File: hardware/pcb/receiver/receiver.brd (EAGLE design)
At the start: 100 x 100 mm, 82 parts, among them X1 5-1634506-1H

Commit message: hw: receiver board changes
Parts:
- removed C17, C23: 100n, rcl:C0805
- removed L6: ferrite bead, inductor-neosid:SM-NE29
- moved R8 148.2 mm to (71.1, 73.7), turned to 180 degrees
- moved C43 142.8 mm to (65.7, 60.5)
- moved R7 141.1 mm to (69.1, 71.1), turned to 180 degrees
- moved C4 140.4 mm to (84.5, 27.1), turned to 270 degrees
- moved C38 139.6 mm to (70.6, 39.7), turned to 90 degrees
- moved C5 133.9 mm to (73.4, 39.6), turned to 90 degrees
- moved C35 132.7 mm to (70.6, 56.9), turned to 90 degrees
- moved C29 129.0 mm to (61.5, 45.7), flipped to the bottom, turned to 180 degrees
- moved C28 126.4 mm to (65.6, 42.3), flipped to the bottom
- moved IC5 125.2 mm to (68.5, 48.0)
- moved C2 122.5 mm to (80.6, 64.8), turned to 180 degrees
- moved L7 122.0 mm to (65.0, 66.4), turned to 180 degrees
- moved C42 122.0 mm to (81.7, 27.4), turned to 270 degrees
- moved C3 121.0 mm to (72.9, 56.6), turned to 270 degrees
- moved C27 118.1 mm to (64.1, 55.2), flipped to the bottom, turned to 90 degrees
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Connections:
- removed net N$35: SV1.2
- net +3V3: no longer C17.2, C42.2, JP1.1, L6.2, R11.2, R12.2, R7.2, V1.8
- net +3V3A_ADC: now also JP1.1, R11.2, R12.2, R7.2; no longer C23.2
- net AMPOUT_N: now also IC2.4, R2.1; no longer IC2.5, R1.1
- net AMPOUT_P: now also IC2.5, R1.1; no longer IC2.4, R2.1
- net ENC: now also SV1.2; no longer SV1.8
- net ENC_N: now also IC5.12; no longer IC5.13
- net ENC_P: now also IC5.13; no longer IC5.12
- net GND: no longer C17.1, C23.1
- net IN_N: now also IC5.9, R2.2; no longer IC5.8, R1.2
- net IN_P: now also IC5.8, R1.2; no longer IC5.9, R2.2
- net N$4: now also IC2.8; no longer IC2.1
- net N$5: now also IC2.1; no longer IC2.8
- net VDD: now also C42.2, V1.8; no longer L6.1
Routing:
- net IN_N: track 0.00 -> 0.55 mm
- added copper zone on layer 1, net GND

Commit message: hw: receiver ferrite beads between capacitors
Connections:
- net +3V3: now also C43.1
- net +3V3A_ADC: no longer C43.1
- net +5V: now also C41.1
- net +5V_AMP: no longer C41.1
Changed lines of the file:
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@@
 <contactref element="L4" pad="1"/>
 <contactref element="L7" pad="2"/>
+<contactref element="C43" pad="1"/>
 <wire x1="77.528" y1="61.266" x2="79.674" y2="64.808" width="0" layer="19" extent="1-1"/>
-<wire x1="63.802" y1="66.428" x2="77.528" y2="61.266" width="0" layer="19" extent="1-1"/>
+<wire x1="64.798" y1="60.46" x2="77.528" y2="61.266" width="0" layer="19" extent="1-1"/>
+<wire x1="63.802" y1="66.428" x2="64.798" y2="60.46" width="0" layer="19" extent="1-1"/>
 <wire x1="47.55" y1="88" x2="63.802" y2="66.428" width="0" layer="19" extent="1-1"/>
 <wire x1="45" y1="88.45" x2="47.55" y2="88" width="0" layer="19" extent="1-1"/>
@@
 <contactref element="C29" pad="2"/>
 <contactref element="L7" pad="1"/>
-<contactref element="C43" pad="1"/>
 <contactref element="IC5" pad="1"/>
 <contactref element="JP1" pad="1"/>
@@
 <wire x1="69.342" y1="67.482" x2="68.138" y2="71.12" width="0" layer="19" extent="1-1"/>
 <wire x1="66.102" y1="66.428" x2="69.342" y2="67.482" width="0" layer="19" extent="1-1"/>
-<wire x1="64.798" y1="60.46" x2="66.102" y2="66.428" width="0" layer="19" extent="1-1"/>
-<wire x1="64.112" y1="56.17" x2="64.798" y2="60.46" width="0" layer="19" extent="1-16"/>
+<wire x1="64.112" y1="56.17" x2="66.102" y2="66.428" width="0" layer="19" extent="1-16"/>
 <wire x1="64.1" y1="51.75" x2="64.112" y2="56.17" width="0" layer="19" extent="1-16"/>
 <wire x1="64.1" y1="49.75" x2="64.1" y2="51.75" width="0" layer="19" extent="1-1"/>
@@
 <contactref element="C8" pad="2"/>
 <contactref element="L5" pad="1"/>
-<contactref element="C41" pad="1"/>
 <contactref element="IC2" pad="3"/>
 <contactref element="IC2" pad="7"/>
 <wire x1="37.274" y1="59.452" x2="39.992" y2="62.914" width="0" layer="19" extent="1-1"/>
-<wire x1="41.19" y1="55.544" x2="37.274" y2="59.452" width="0" layer="19" extent="1-1"/>
-<wire x1="47.635" y1="50.17" x2="41.19" y2="55.544" width="0" layer="19" extent="1-1"/>
+<wire x1="47.635" y1="50.17" x2="37.274" y2="59.452" width="0" layer="19" extent="1-1"/>
 <wire x1="48.285" y1="45.83" x2="47.635" y2="50.17" width="0" layer="19" extent="1-1"/>
 </signal>
@@
 <contactref element="C30" pad="2"/>
 <contactref element="L5" pad="2"/>
+<contactref element="C41" pad="1"/>
 <wire x1="40.96" y1="90.9" x2="42.23" y2="90.9" width="0" layer="19" extent="1-1"/>
 <wire x1="41.5" y1="88.45" x2="40.96" y2="90.9" width="0" layer="19" extent="1-1"/>
@@
 <wire x1="21.5" y1="90.95" x2="21.5" y2="94.05" width="0" layer="19" extent="1-1"/>
 <wire x1="39.992" y1="65.214" x2="39" y2="88.45" width="0" layer="19" extent="1-1"/>
+<wire x1="41.19" y1="55.544" x2="39.992" y2="65.214" width="0" layer="19" extent="1-1"/>
 </signal>
 <signal name="N$12">

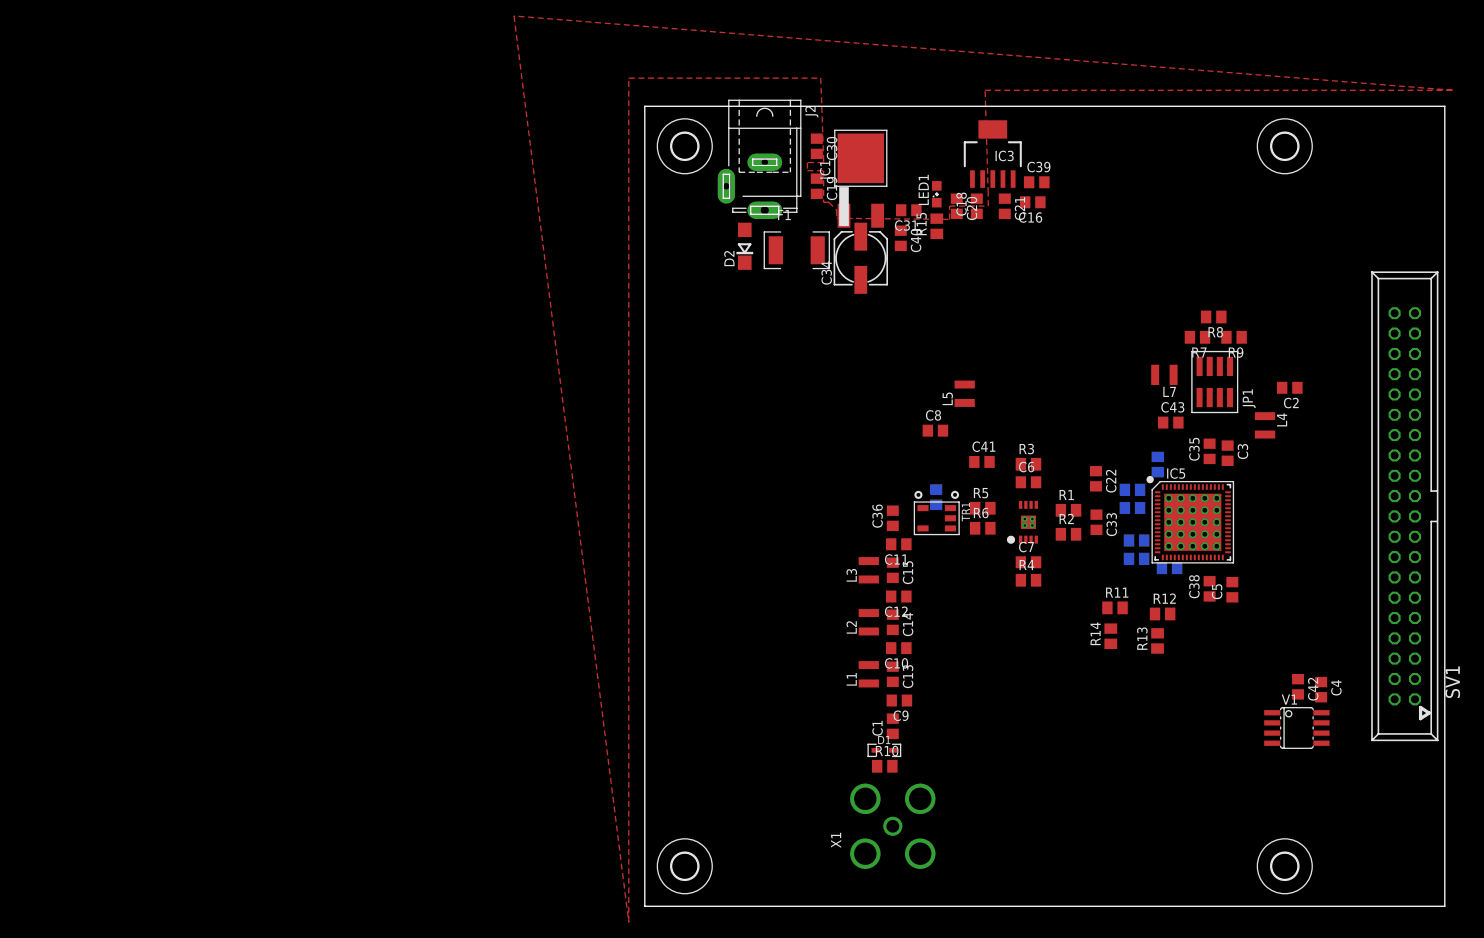
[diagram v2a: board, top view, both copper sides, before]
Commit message: hw: modified adc input clock resistors resistors
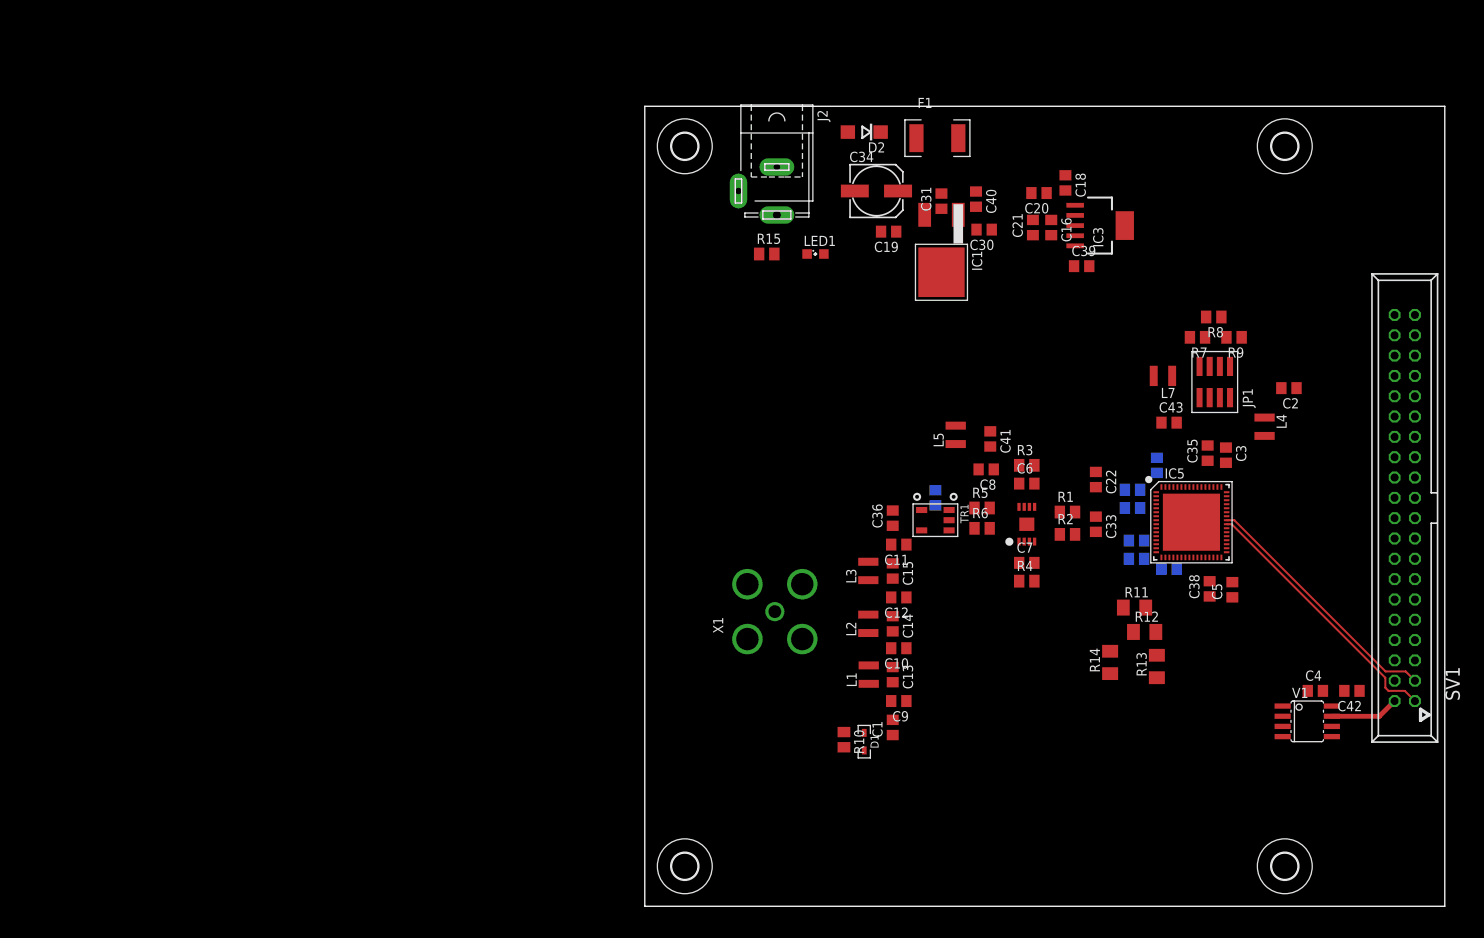
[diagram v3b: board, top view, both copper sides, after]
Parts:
- R11, R12, R13, R14: device rcl:M0805 -> rcl:M1206
- moved X1 30.6 mm to (16.3, 36.8)
- moved C30 23.4 mm to (42.4, 84.6), turned to 180 degrees
- moved F1 22.5 mm to (36.6, 96.0)
- moved R15 21.5 mm to (15.2, 81.5), turned to 0 degrees
- moved D2 20.7 mm to (27.4, 96.8), turned to 180 degrees
- moved IC1 17.5 mm to (37.1, 79.2), turned to 90 degrees
- moved LED1 16.9 mm to (21.3, 81.5), turned to 0 degrees
- moved IC3 16.1 mm to (56.9, 85.1), turned to 270 degrees
- moved C39 11.9 mm to (54.6, 80.0)
- moved C18 11.5 mm to (52.6, 90.4), turned to 270 degrees
- moved C19 10.6 mm to (30.5, 84.3), turned to 180 degrees
- moved C40 10.6 mm to (41.4, 88.4)
- moved C20 10.4 mm to (49.3, 89.2), turned to 180 degrees
- moved C34 8.63 mm to (29.0, 89.4), turned to 0 degrees
- moved C8 7.98 mm to (42.7, 54.6), turned to 180 degrees
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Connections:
- removed net CLKOUTA: IC5.41, SV1.1
- removed net CLKOUTB: IC5.40, SV1.3
- removed net N$10: SV1.14
- removed net N$11: SV1.10
- removed net N$24: SV1.13
- removed net N$26: SV1.9
- removed net N$29: SV1.7
- removed net N$30: SV1.5
- new net CLKOUT_N: IC5.40, SV1.1
- new net CLKOUT_P: IC5.41, SV1.3
- net OFA: no longer SV1.21
- net PGA: no longer SV1.15
- net RAND: no longer SV1.17
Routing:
- net CLKOUT_N: track 0.00 -> 33.4 mm
- net CLKOUT_P: track 0.00 -> 31.8 mm
- net ENC: track 0.00 -> 8.64 mm
- removed copper zone on layer 1, net GND

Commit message: hw: board updates
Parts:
- moved L5 23.8 mm to (53.8, 40.4), flipped to the bottom, turned to 180 degrees
- moved C8 16.0 mm to (53.6, 42.9), flipped to the bottom, turned to 0 degrees
- moved C43 13.1 mm to (58.7, 71.6)
- moved C2 13.0 mm to (80.0, 77.7)
- moved L7 12.9 mm to (57.1, 76.7)
- moved C10 11.5 mm to (38.4, 22.9)
- moved C9 11.5 mm to (38.4, 16.3)
- moved L1 11.5 mm to (34.6, 19.6)
- moved C1 11.3 mm to (37.3, 13.0)
- moved C13 11.3 mm to (37.3, 19.6)
- moved C11 11.3 mm to (38.4, 36.1)
- moved C12 11.3 mm to (38.4, 29.5)
- moved L2 11.3 mm to (34.5, 26.2)
- moved L3 11.3 mm to (34.5, 32.8)
- moved C36 11.1 mm to (37.3, 39.4)
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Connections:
- net VCC3P3 renamed N$48
- net VCC_SYS renamed N$58
- removed net N$34: SV1.4
- new net N$32: SV1.36
- new net N$35: SV1.38
- new net N$36: SV1.40
- new net N$37: SV1.39
- new net N$38: SV1.37
- new net N$45: SV1.35
- new net N$46: SV1.33
- new net N$52: SV1.5
- net DA0: now also SV1.13
- net DA1: now also SV1.14
- net DA10: now also SV1.23
- net DA11: now also SV1.24
- net DA12: now also SV1.25
- net DA13: now also SV1.26
- net DA14: now also SV1.27
- net DA15: now also SV1.28
- net DA2: now also SV1.15
- net DA3: now also SV1.16
- net DA4: now also SV1.17
- net DA5: now also SV1.18
- net DA6: now also SV1.19
- net DA7: now also SV1.20
- net DA8: now also SV1.21
- net DA9: now also SV1.22
- net DITH: now also SV1.4
- net OFA: now also SV1.32
- net PGA: now also SV1.34
- net RAND: now also SV1.31
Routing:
- net VDD: track 0.00 -> 58.8 mm, vias 0 -> 3
- net N$2: track 0.00 -> 40.4 mm
- net ENC_N: track 0.00 -> 38.6 mm
- net RAND: track 0.00 -> 34.8 mm
- net ENC_P: track 0.00 -> 34.1 mm
- net PGA: track 0.00 -> 33.3 mm
- net GND: track 0.00 -> 31.6 mm, vias 0 -> 2
- net DITH: track 0.00 -> 30.4 mm, vias 0 -> 2
- net DA14: track 0.00 -> 29.8 mm
- net OFA: track 0.00 -> 29.1 mm
- net DA12: track 0.00 -> 28.2 mm
- net DA15: track 0.00 -> 27.5 mm
- net DA10: track 0.00 -> 26.7 mm
- net DA13: track 0.00 -> 25.9 mm
- net DA8: track 0.00 -> 25.3 mm
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
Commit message: hw: board
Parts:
- moved L5 46.4 mm to (22.4, 74.4)
- moved X1 29.0 mm to (23.1, 58.4)
- moved R10 25.4 mm to (22.2, 43.8)
- moved D1 21.9 mm to (22.1, 35.8)
- moved L7 15.5 mm to (57.9, 61.2)
- moved R15 11.7 mm to (23.6, 89.7), turned to 270 degrees
- moved JP1 7.15 mm to (68.8, 68.1)
- moved R9 7.06 mm to (69.3, 74.7)
- moved R8 7.05 mm to (66.9, 77.2)
- moved L4 6.41 mm to (80.0, 71.9)
- moved C43 6.40 mm to (57.9, 65.3)
- moved C11 6.35 mm to (36.6, 42.2)
- moved C12 6.35 mm to (36.6, 35.6)
- moved C14 6.35 mm to (35.6, 32.3)
- moved C15 6.35 mm to (35.6, 38.9)
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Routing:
- net +3V3: track 5.31 -> 63.7 mm
- net GND: track 31.6 -> 82.8 mm, vias 2 -> 6
- net +3V3A_ADC: track 12.5 -> 47.9 mm, vias 6 -> 5
- net N$2: track 40.4 -> 55.5 mm
- net N$9: track 0.00 -> 7.94 mm
- net N$6: track 0.00 -> 7.85 mm
- net +5V: track 23.8 -> 29.1 mm
- net N$3: track 10.7 -> 6.41 mm
- net N$12: track 4.10 -> 0.00 mm
- net +5V_AMP: track 3.13 -> 6.79 mm, vias 1 -> 2
- net VDD: track 58.8 -> 61.9 mm
- net MODE: track 22.0 -> 19.2 mm
- net N$7: track 16.0 -> 18.6 mm
- net N$20: track 14.9 -> 17.2 mm

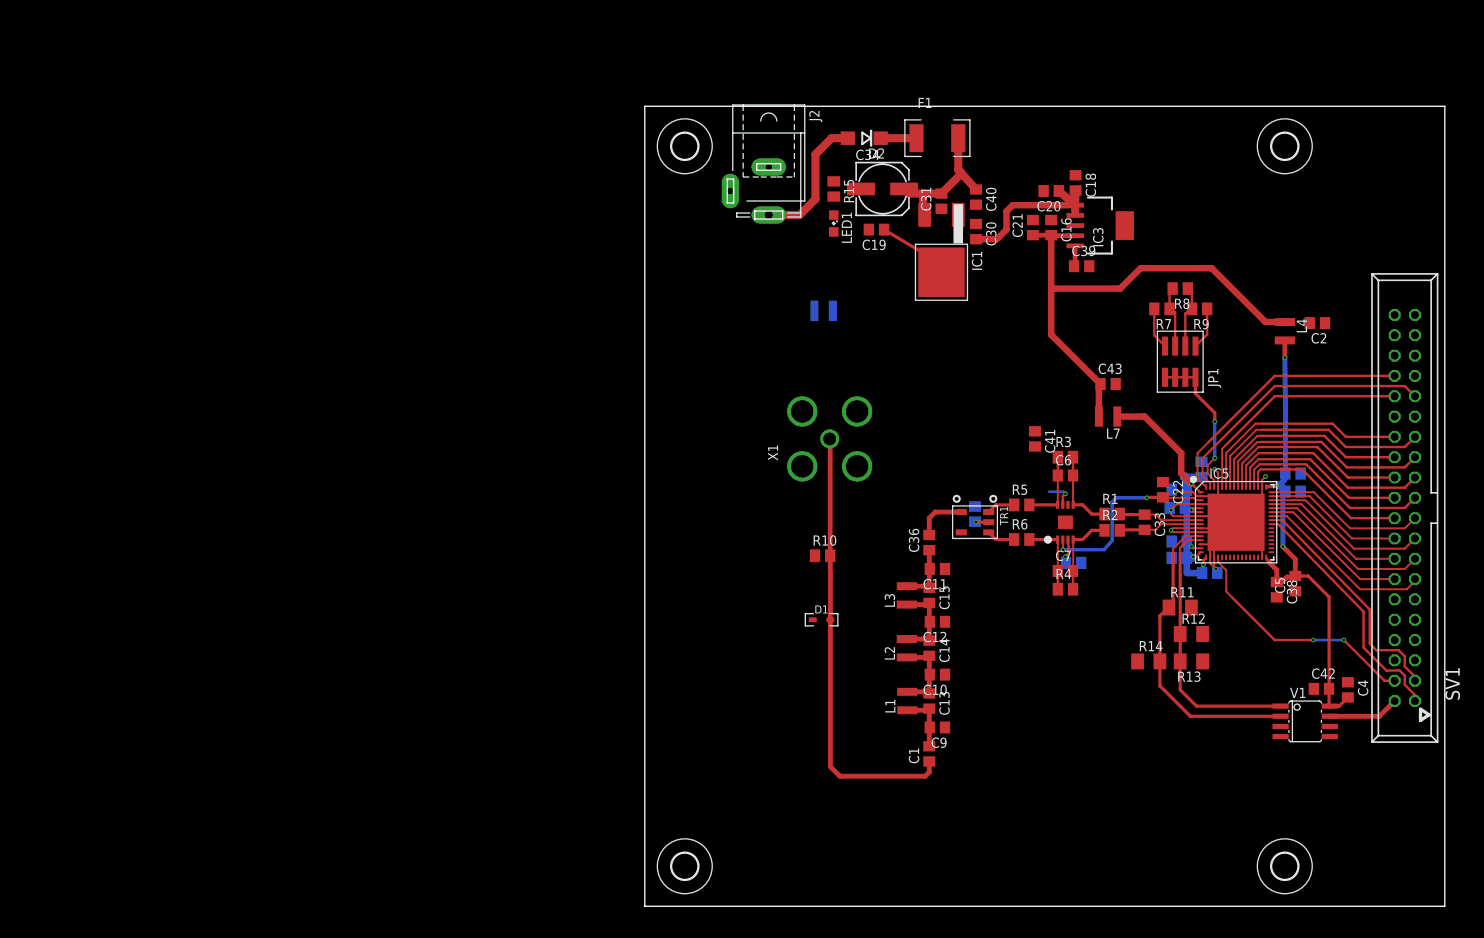
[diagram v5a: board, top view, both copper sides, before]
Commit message: hw: ground plane
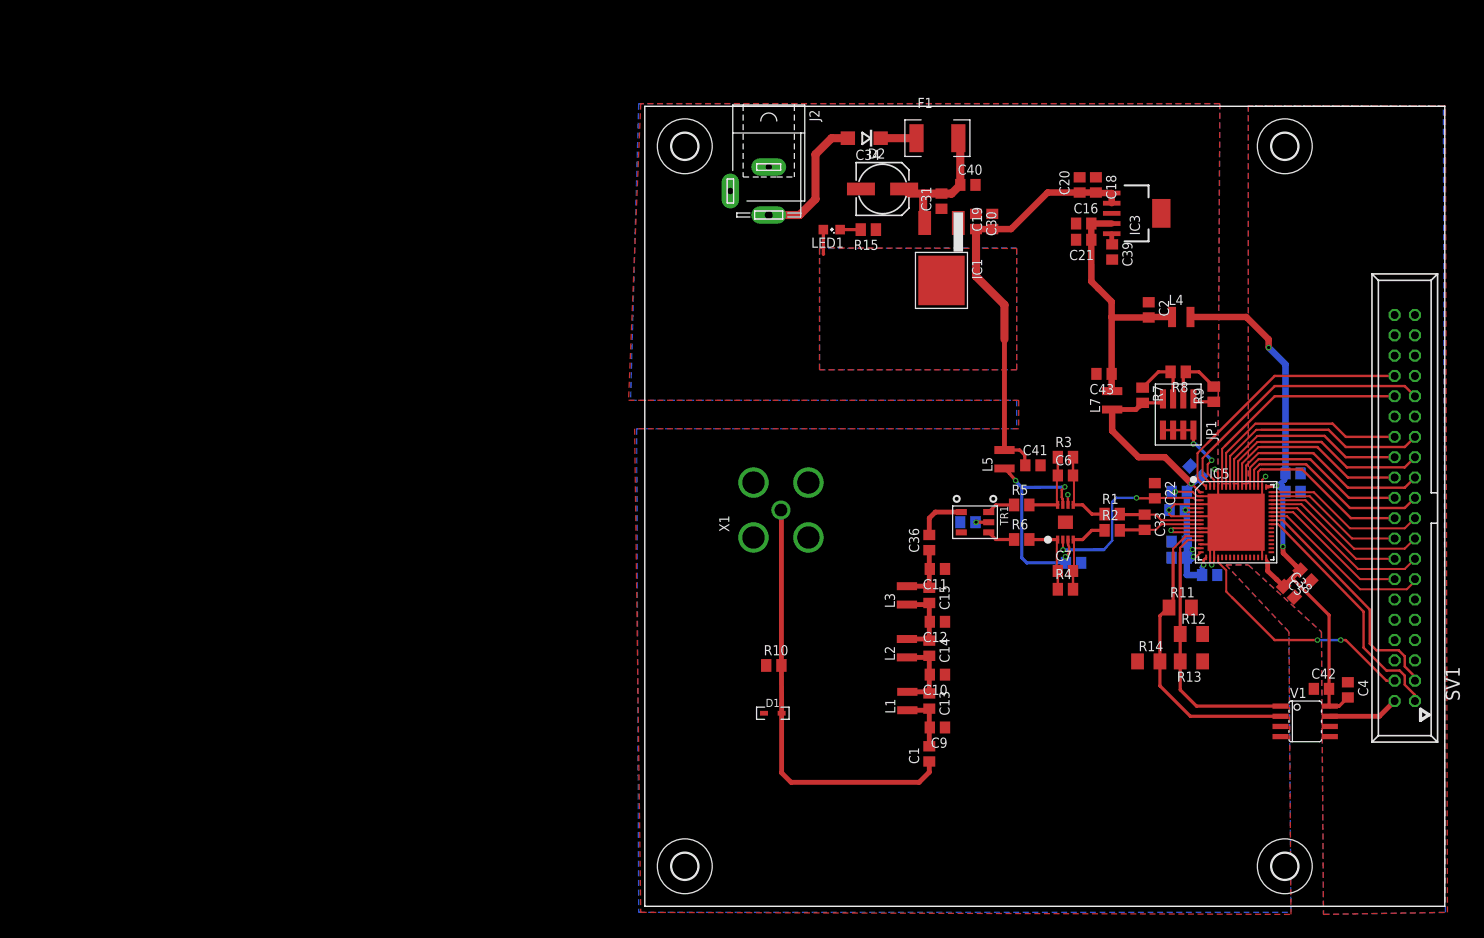
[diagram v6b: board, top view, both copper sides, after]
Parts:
- moved L5 29.2 mm to (45.0, 55.9), flipped to the top, turned to 90 degrees
- moved C2 21.1 mm to (63.0, 74.5), turned to 270 degrees
- moved R10 15.0 mm to (16.1, 30.1)
- moved C19 14.5 mm to (43.4, 85.6), turned to 90 degrees
- moved D1 13.2 mm to (16.0, 24.1)
- moved L4 13.1 mm to (67.1, 73.7), turned to 0 degrees
- moved R7 11.1 mm to (62.2, 63.9), turned to 270 degrees
- moved R9 10.8 mm to (71.1, 64.0), turned to 90 degrees
- moved X1 10.8 mm to (17.0, 49.5)
- moved R8 10.4 mm to (66.7, 66.8)
- moved R15 6.67 mm to (27.9, 84.6), turned to 180 degrees
- moved JP1 6.61 mm to (68.6, 61.5)
- moved C21 6.53 mm to (54.9, 83.3), turned to 180 degrees
- moved IC3 4.82 mm to (61.5, 86.6)
- moved C39 4.20 mm to (58.4, 81.8), turned to 270 degrees
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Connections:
- net N$20 renamed 12-18V
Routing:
- net +3V3: track 63.7 -> 32.2 mm
- net +5V: track 29.1 -> 56.9 mm
- net +5V_AMP: track 6.79 -> 28.8 mm, vias 2 -> 3
- net VDD: track 61.9 -> 73.5 mm
- net MODE: track 19.2 -> 12.6 mm
- net GND: track 82.8 -> 80.2 mm, vias 6 -> 7
- net N$12: track 0.00 -> 2.57 mm
- net +3V3A_ADC: track 47.9 -> 49.9 mm
- net N$2: track 55.5 -> 53.7 mm
- net N$19: track 2.60 -> 1.36 mm
- net N$7: track 18.6 -> 17.3 mm
- net N$5: track 9.76 -> 10.3 mm
- added copper zone on layer 1, net +5V
- added copper zone on layer 16, net +5V
- added copper zone on layer 1, net GND
- added copper zone on layer 16, net GND
